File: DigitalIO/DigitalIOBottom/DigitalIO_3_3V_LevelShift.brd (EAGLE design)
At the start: 64 x 82 mm, 72 parts, among them IC1 MCP23017SP, IC2 ULN2803A, K5 HF46105, K6 HF46105, K7 HF46105, K8 HF46105, P1 DF11-06-2DSA, Q1 BS170, Q2 BS170, Q5 691131710002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

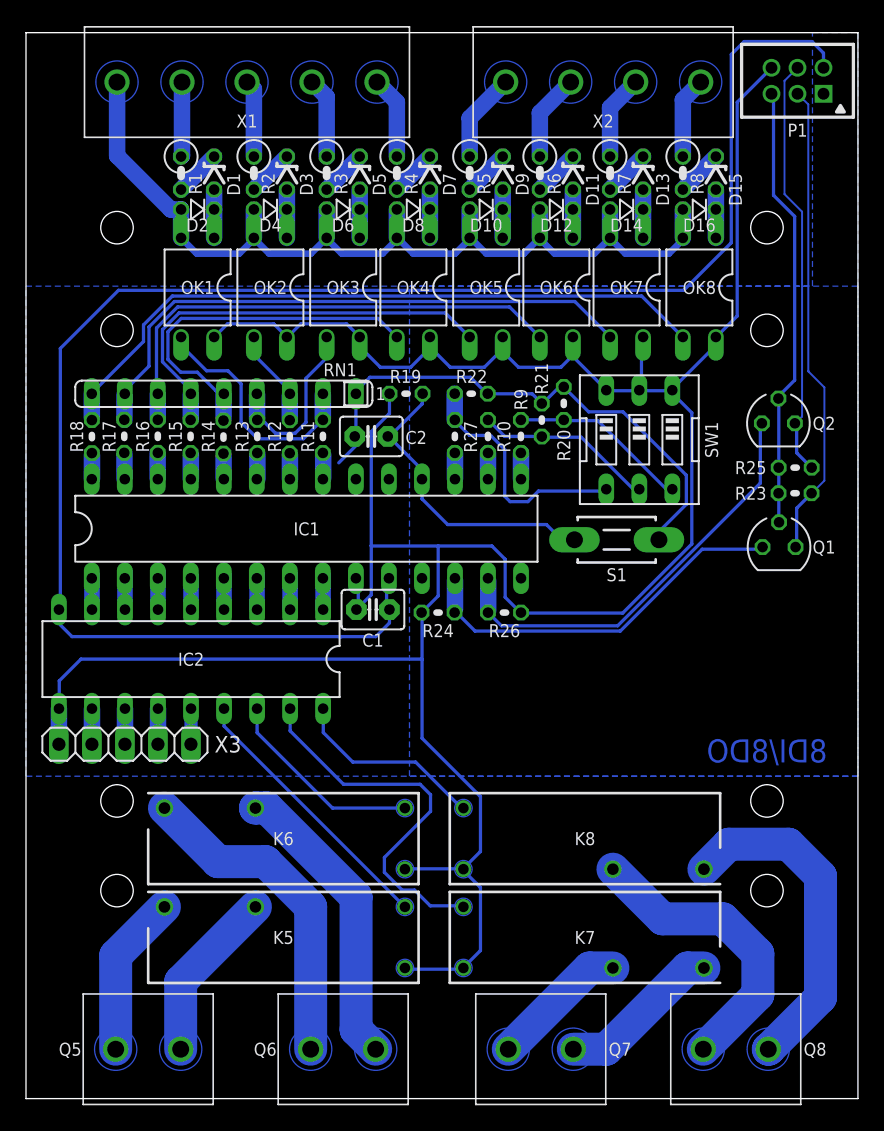
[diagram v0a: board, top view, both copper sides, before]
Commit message: Increase drill from 2.5mm to 2.75mm. Remove not need holes.
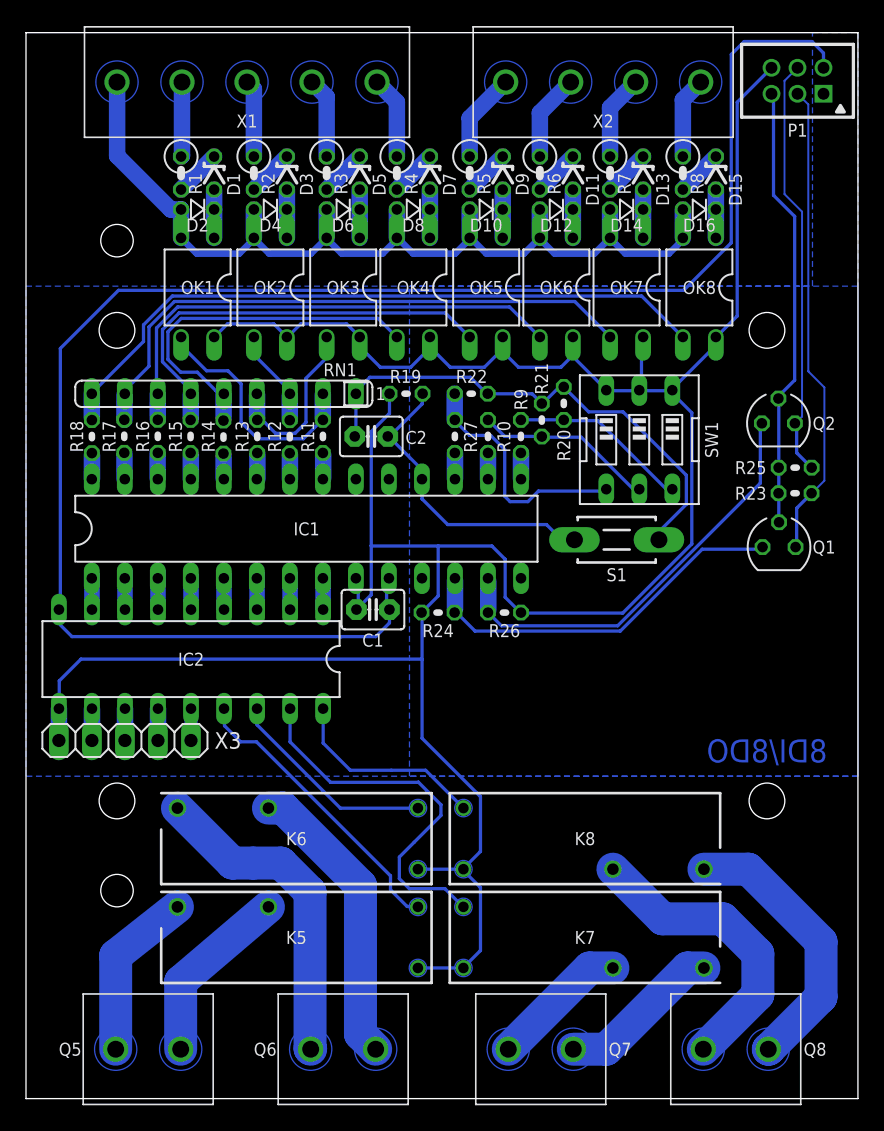
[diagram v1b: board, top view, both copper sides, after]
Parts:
- moved K5 1.00 mm to (20.8, 12.4)
- moved K6 1.00 mm to (20.8, 20.0)
- moved X3 0.29 mm to (7.61, 27.6)
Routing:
- net N$38: track 25.8 -> 21.3 mm
- net GND: track 173.0 -> 170.5 mm
- net +5V: track 224.4 -> 222.7 mm
- net N$42: track 21.0 -> 22.6 mm
- net N$66: track 12.5 -> 13.3 mm
- net N$75: track 13.3 -> 14.1 mm
- net N$48: track 15.6 -> 16.3 mm
